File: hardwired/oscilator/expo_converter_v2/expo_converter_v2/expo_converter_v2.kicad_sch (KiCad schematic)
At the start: 13 parts, among them Q1 2SC1815, Q2 2SC1815, U1 LM358

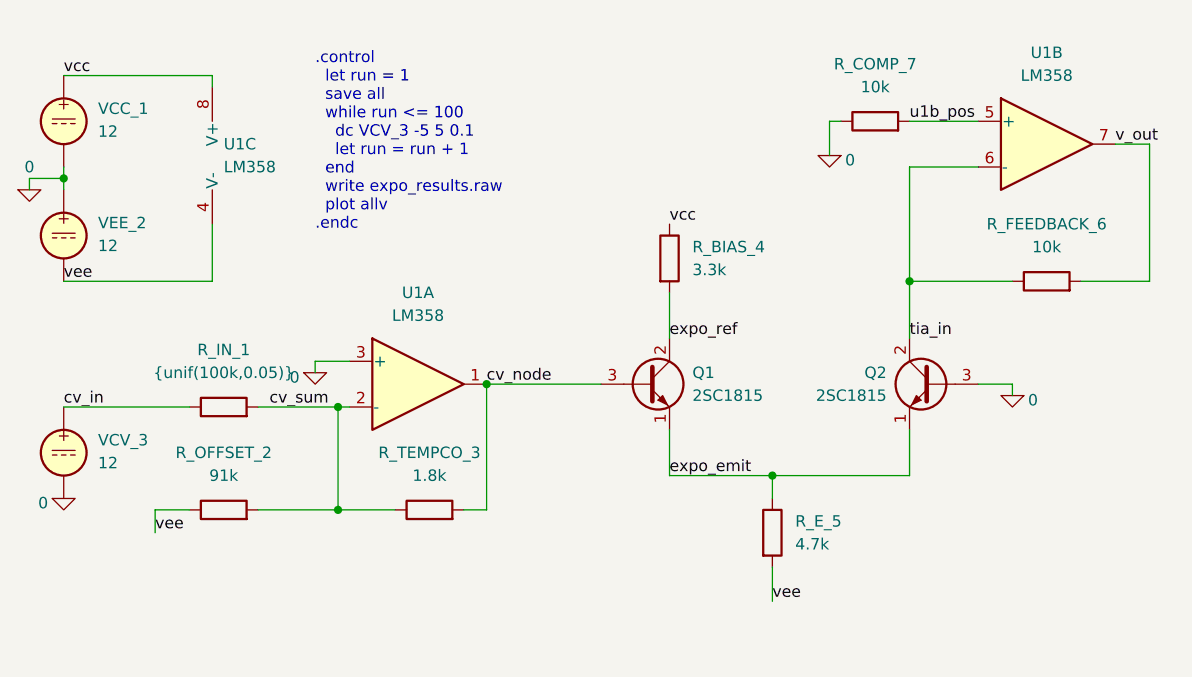
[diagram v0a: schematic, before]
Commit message: increased voltage output to make it eaiser to measure.  added tuning and trouble shooting notes.
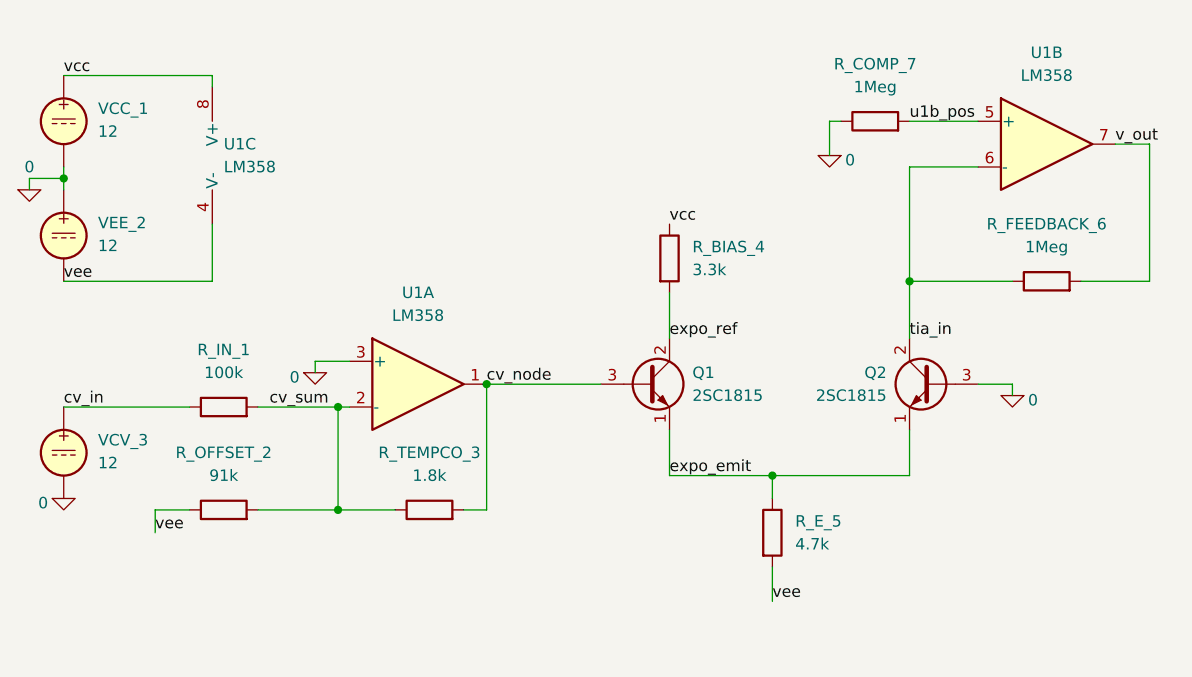
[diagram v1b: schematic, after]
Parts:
- R_COMP_7, R_FEEDBACK_6: value 10k -> 1Meg
- R_IN_1: value {unif(100k,0.05)} -> 100k
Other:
- note removed: ".control let run = 1 save all while run <= 100 dc VCV_3 -5 5 0.1 let run = run + 1 end write expo_results.raw plot allv .endc"
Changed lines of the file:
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@@
 	(generator_version "10.0")
 	(paper "A4")
-	(text ".control\n  let run = 1\n  save all\n  while run <= 100\n    dc VCV_3 -5 5 0.1\n    let run = run + 1\n  end\n  write expo_results.raw\n  plot allv\n.endc"
-		(exclude_from_sim no)
-		(at 57.15 35.306 0)
-		(effects
-			(font
-				(size 1.27 1.27)
-			)
-			(justify left)
-		)
-	)
 	(junction
 		(at 107.95 72.39)
@@
 			)
 		)
-		(property "Value" "{unif(100k,0.05)}"
+		(property "Value" "100k"
 			(at 46.99 60.96 90)
 			(show_name no)
@@
 			)
 		)
-		(property "Value" "10k"
+		(property "Value" "1Meg"
 			(at 138.43 46.99 90)
 			(show_name no)
@@
 			)
 		)
-		(property "Value" "10k"
+		(property "Value" "1Meg"
 			(at 119.38 29.21 90)
 			(show_name no)

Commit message: minor design tweaks.
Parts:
- R_COMP_7, R_FEEDBACK_6: value 1Meg -> 100k
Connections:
- net vcc renamed +12V
- net vee renamed -12V
